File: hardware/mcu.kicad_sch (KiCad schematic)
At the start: 17 parts, among them J301 TagConnect, U301 STM32G431, U302 SN65HVD230, Y301 12MHz

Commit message: firmware defines
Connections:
- net MOT_EN_A: no longer names the net of U301.30 (PA8)
- net MOT_EN_B: no longer names the net of U301.29 (PC6)
- no-connect marks 14 -> 16
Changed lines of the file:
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@@
   (no_connect (at 83.82 125.73))
   (no_connect (at 187.96 72.39))
+  (no_connect (at 116.84 90.17))
+  (no_connect (at 83.82 90.17))
   (no_connect (at 96.52 64.77))
   (no_connect (at 83.82 123.19))
@@
     (stroke (width 0) (type default))
   )
-  (wire (pts (xy 73.66 90.17) (xy 83.82 90.17))
-    (stroke (width 0) (type default))
-  )
-  (wire (pts (xy 116.84 90.17) (xy 128.27 90.17))
-    (stroke (width 0) (type default))
-  )
   (wire (pts (xy 101.6 50.8) (xy 101.6 64.77))
     (stroke (width 0) (type default))
@@
     (effects (font (size 1.27 1.27)) (justify left))
   )
-  (hierarchical_label "MOT_EN_B" (shape output) (at 73.66 90.17 180) (fields_autoplaced)
-    (effects (font (size 1.27 1.27)) (justify right))
-  )
   (hierarchical_label "TIM2_CH2" (shape output) (at 128.27 72.39 0) (fields_autoplaced)
     (effects (font (size 1.27 1.27)) (justify left))
@@
     (effects (font (size 1.27 1.27)) (justify right))
   )
-  (hierarchical_label "MOT_EN_A" (shape output) (at 128.27 90.17 0) (fields_autoplaced)
-    (effects (font (size 1.27 1.27)) (justify left))
-  )
   (hierarchical_label "TIM3_CH2" (shape input) (at 73.66 118.11 180) (fields_autoplaced)

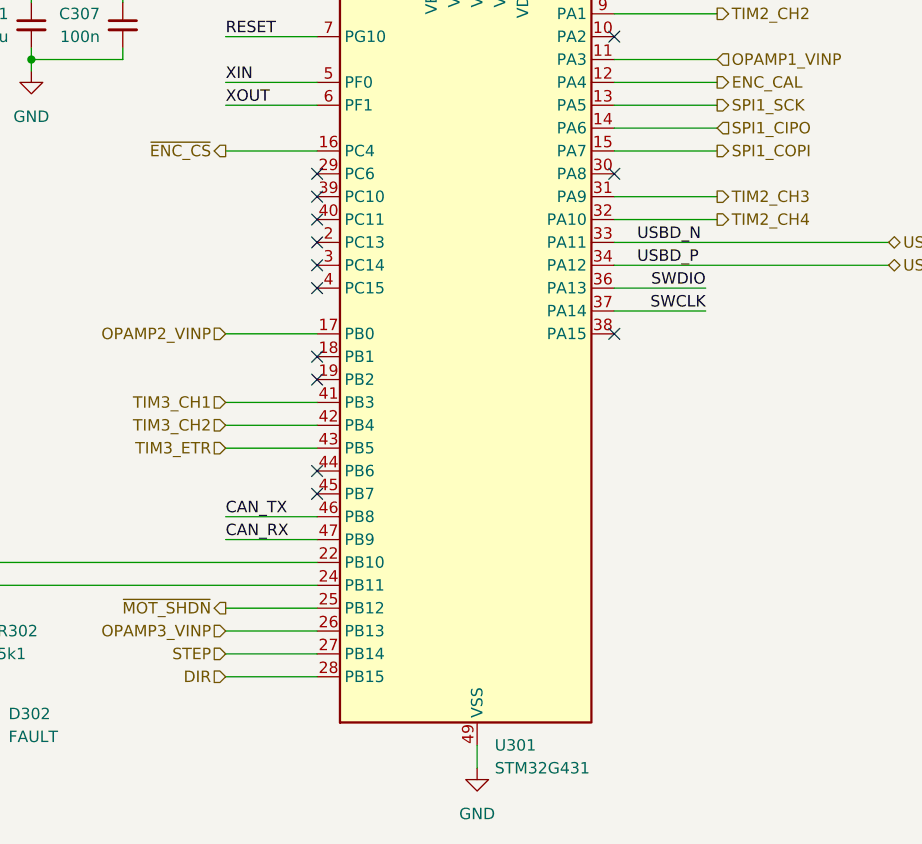
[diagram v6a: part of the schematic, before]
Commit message: change pins to support I2C input
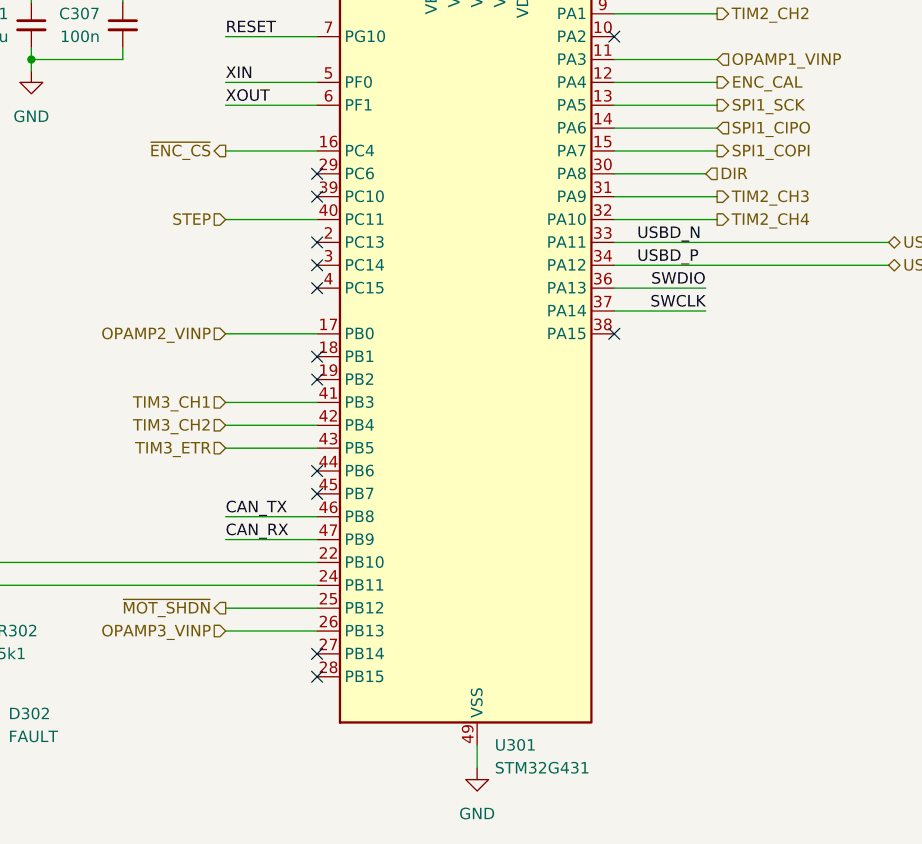
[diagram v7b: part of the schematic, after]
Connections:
- net DIR: now also U301.30 (PA8); no longer U301.28 (PB15)
- net STEP: now also U301.40 (PC11); no longer U301.27 (PB14)
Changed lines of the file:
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@@
   (junction (at 198.12 81.28) (diameter 0) (color 0 0 0 0)
   )
-  (no_connect (at 83.82 95.25))
   (no_connect (at 242.57 74.93))
+  (no_connect (at 83.82 146.05))
   (no_connect (at 83.82 92.71))
+  (no_connect (at 83.82 143.51))
   (no_connect (at 116.84 107.95))
   (no_connect (at 116.84 74.93))
@@
   (no_connect (at 83.82 125.73))
   (no_connect (at 187.96 72.39))
-  (no_connect (at 116.84 90.17))
   (no_connect (at 83.82 90.17))
   (no_connect (at 96.52 64.77))
@@
     (stroke (width 0) (type default))
   )
-  (wire (pts (xy 73.66 143.51) (xy 83.82 143.51))
+  (wire (pts (xy 73.66 95.25) (xy 83.82 95.25))
     (stroke (width 0) (type default))
   )
@@
     (stroke (width 0) (type default))
   )
-  (wire (pts (xy 73.66 146.05) (xy 83.82 146.05))
+  (wire (pts (xy 127 90.17) (xy 116.84 90.17))
     (stroke (width 0) (type default))
   )
@@
     (effects (font (size 1.27 1.27)) (justify left))
   )
-  (hierarchical_label "STEP" (shape input) (at 73.66 143.51 180) (fields_autoplaced)
+  (hierarchical_label "STEP" (shape input) (at 73.66 95.25 180) (fields_autoplaced)
     (effects (font (size 1.27 1.27)) (justify right))
   )
@@
     (effects (font (size 1.27 1.27)) (justify right))
   )
-  (hierarchical_label "DIR" (shape input) (at 73.66 146.05 180) (fields_autoplaced)
-    (effects (font (size 1.27 1.27)) (justify right))
+  (hierarchical_label "DIR" (shape input) (at 127 90.17 0) (fields_autoplaced)
+    (effects (font (size 1.27 1.27)) (justify left))
   )
   (symbol (lib_id "Device:R_Small_US") (at 252.73 110.49 0) (mirror y) (unit 1)

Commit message: fix bringup issues
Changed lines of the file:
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@@
     (stroke (width 0) (type default))
   )
-  (wire (pts (xy 83.82 87.63) (xy 73.66 87.63))
+  (wire (pts (xy 73.66 87.63) (xy 83.82 87.63))
     (stroke (width 0) (type default))
   )
